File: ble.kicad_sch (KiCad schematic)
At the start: 0 parts

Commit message: schema functionally done
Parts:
- added C19, C21: 12pF, Capacitor_SMD:C_0805_2012Metric, symbol Device:C
- added C22: 100nF, Capacitor_SMD:C_0805_2012Metric, symbol Device:C
- added C23: 4.7uF, Capacitor_SMD:C_0805_2012Metric, symbol Device:C
- added MOD1: BT832A, footprints:BT832A, symbol user:BT832A
- added Y1: FC-135 32.7680KA-AC0, Crystal:Crystal_SMD_3215-2Pin_3.2x1.5mm, symbol Device:Crystal
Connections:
- new net: C21.2, MOD1.4 (P001/XL2), Y1.1
- new net: C19.2, MOD1.3 (P000/XL1), Y1.2
- new net +3V0: C22.1, C23.1, MOD1.9 (VDD)
- new net BLE_RESET: MOD1.14 (P021/RESET)
- new net BLE_SCL: MOD1.2 (P027/SCL)
- new net BLE_SDA: MOD1.1 (P026/SDA)
- new net GND: C19.1, C21.1, C22.2, C23.2, MOD1.10 (GND)
- new net SWCLK: MOD1.15 (SWCLK)
- new net SWD: MOD1.16 (SWDIO)
- no-connect marks 0 -> 7

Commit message: reannotation
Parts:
- renumbered C19 to C21, C21 to C22, C22 to C23, C23 to C24, Y1 to Y2

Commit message: schematic cleanup
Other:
- moved on the sheet: C21, C23, C24, Y2

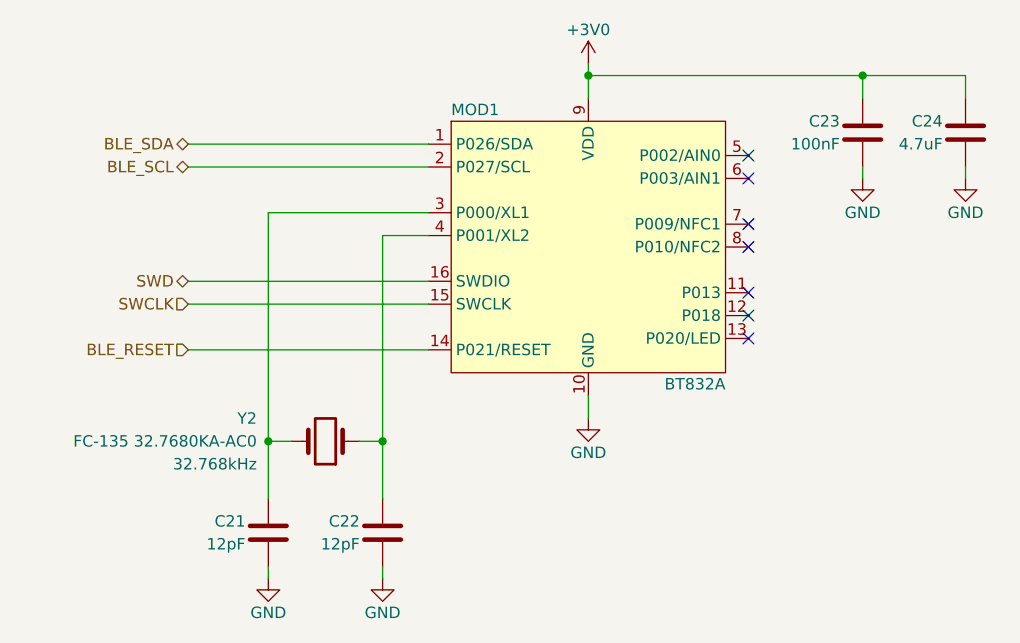
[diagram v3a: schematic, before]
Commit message: added testpoints
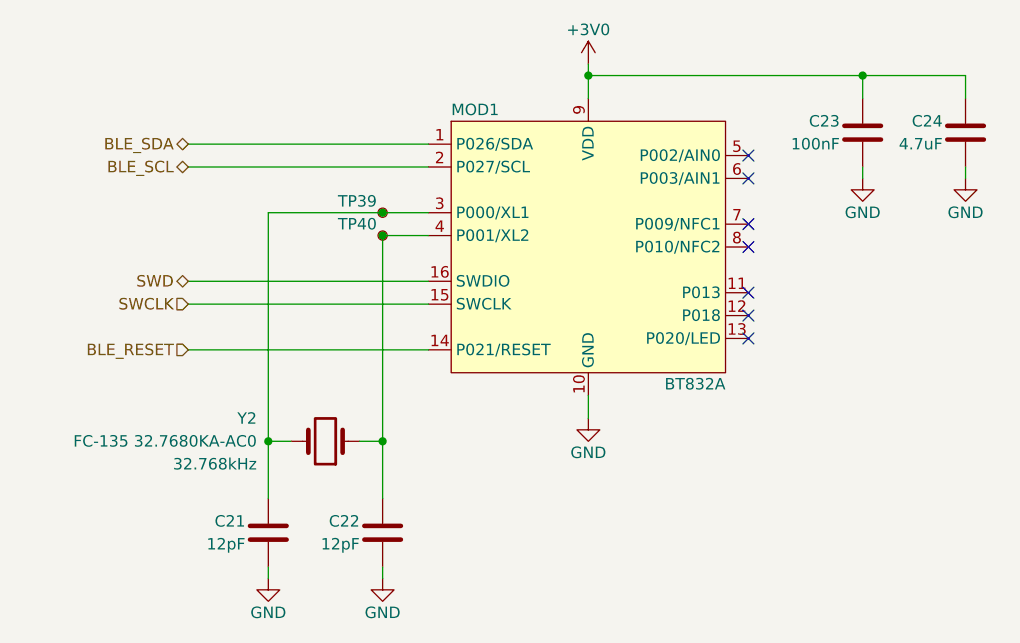
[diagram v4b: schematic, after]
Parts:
- added TP39, TP40: TestPoint_Small, TestPoint:TestPoint_Pad_D2.0mm, symbol Connector:TestPoint_Small
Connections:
- net at C22.2, MOD1.4 (P001/XL2), Y2.1: now also TP40.1
- net at C21.2, MOD1.3 (P000/XL1), Y2.2: now also TP39.1

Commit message: test points
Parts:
- removed TP39, TP40: TestPoint_Small, TestPoint:TestPoint_Pad_D2.0mm, symbol Connector:TestPoint_Small
- added TP48: BX1, TestPoint:TestPoint_Pad_D2.0mm, symbol Connector:TestPoint_Small
- added TP49: BX2, TestPoint:TestPoint_Pad_D2.0mm, symbol Connector:TestPoint_Small
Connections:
- net at C22.2, MOD1.4 (P001/XL2), Y2.1: now also TP49.1
- net at C21.2, MOD1.3 (P000/XL1), Y2.2: now also TP48.1

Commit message: GPIO shuffling + reannotate
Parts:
- renumbered TP48 to TP49, TP49 to TP50
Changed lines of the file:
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@@
   (symbol (lib_id "Connector:TestPoint_Small") (at 123.19 91.44 0) (mirror y) (unit 1)
     (in_bom yes) (on_board yes) (dnp no)
-    (property "Reference" "TP48" (at 122.555 90.17 0)
+    (property "Reference" "TP49" (at 122.555 90.17 0)
       (effects (font (size 1.27 1.27)) (justify left) hide)
     )
@@
       (project "gkos_pebble"
         (path "/ab6fff6e-44fa-4992-ab9d-8d9a7df4367d/f1e179d9-6d1d-4136-839e-ba1cd3485093"
-          (reference "TP48") (unit 1)
+          (reference "TP49") (unit 1)
         )
       )
@@
   (symbol (lib_id "Connector:TestPoint_Small") (at 123.19 93.98 0) (mirror y) (unit 1)
     (in_bom yes) (on_board yes) (dnp no)
-    (property "Reference" "TP49" (at 122.555 92.71 0)
+    (property "Reference" "TP50" (at 122.555 92.71 0)
       (effects (font (size 1.27 1.27)) (justify left) hide)
     )
@@
       (project "gkos_pebble"
         (path "/ab6fff6e-44fa-4992-ab9d-8d9a7df4367d/f1e179d9-6d1d-4136-839e-ba1cd3485093"
-          (reference "TP49") (unit 1)
-        )
-      )
+          (reference "TP50") (unit 1)
+        )
+      )

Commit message: in progress pcb
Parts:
- C21, C22, C23, C24: footprint Capacitor_SMD:C_0805_2012Metric -> Capacitor_SMD:C_0603_1608Metric
- TP49, TP50: footprint TestPoint:TestPoint_Pad_D2.0mm -> TestPoint:TestPoint_Pad_D1.0mm
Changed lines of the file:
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@@
       (effects (font (size 1.27 1.27)) (justify left))
     )
-    (property "Footprint" "TestPoint:TestPoint_Pad_D2.0mm" (at 118.11 91.44 0)
+    (property "Footprint" "TestPoint:TestPoint_Pad_D1.0mm" (at 118.11 91.44 0)
       (effects (font (size 1.27 1.27)) hide)
     )
@@
       (effects (font (size 1.27 1.27)) (justify right))
     )
-    (property "Footprint" "Capacitor_SMD:C_0805_2012Metric" (at 111.4552 123.19 0)
+    (property "Footprint" "Capacitor_SMD:C_0603_1608Metric" (at 111.4552 123.19 0)
       (effects (font (size 1.27 1.27)) hide)
     )
@@
       (effects (font (size 1.27 1.27)) (justify right))
     )
-    (property "Footprint" "Capacitor_SMD:C_0805_2012Metric" (at 188.9252 86.36 0)
+    (property "Footprint" "Capacitor_SMD:C_0603_1608Metric" (at 188.9252 86.36 0)
       (effects (font (size 1.27 1.27)) hide)
     )
@@
       (effects (font (size 1.27 1.27)) (justify right))
     )
-    (property "Footprint" "Capacitor_SMD:C_0805_2012Metric" (at 124.1552 123.19 0)
+    (property "Footprint" "Capacitor_SMD:C_0603_1608Metric" (at 124.1552 123.19 0)
       (effects (font (size 1.27 1.27)) hide)
     )
@@
       (effects (font (size 1.27 1.27)) (justify right))
     )
-    (property "Footprint" "Capacitor_SMD:C_0805_2012Metric" (at 177.4952 86.36 0)
+    (property "Footprint" "Capacitor_SMD:C_0603_1608Metric" (at 177.4952 86.36 0)
       (effects (font (size 1.27 1.27)) hide)
     )
@@
       (effects (font (size 1.27 1.27)) (justify left))
     )
-    (property "Footprint" "TestPoint:TestPoint_Pad_D2.0mm" (at 118.11 93.98 0)
-      (effects (font (size 1.27 1.27)) hide)
-    )
+    (property "Footprint" "TestPoint:TestPoint_Pad_D1.0mm" (at 118.11 93.98 0)
+      (effects (font (size 1.27 1.27)) hide)
+    )

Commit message: add the dang eeprom
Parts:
- renumbered TP49 to TP48, TP50 to TP49
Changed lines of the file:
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@@
   (symbol (lib_id "power:+3V0") (at 146.05 74.93 0) (unit 1)
     (in_bom yes) (on_board yes) (dnp no)
-    (property "Reference" "#PWR034" (at 146.05 78.74 0)
+    (property "Reference" "#PWR036" (at 146.05 78.74 0)
       (effects (font (size 1.27 1.27)) hide)
     )
@@
       (project "gkos_pebble"
         (path "/ab6fff6e-44fa-4992-ab9d-8d9a7df4367d/f1e179d9-6d1d-4136-839e-ba1cd3485093"
-          (reference "#PWR034") (unit 1)
+          (reference "#PWR036") (unit 1)
         )
       )
@@
   (symbol (lib_id "Connector:TestPoint_Small") (at 123.19 91.44 0) (mirror y) (unit 1)
     (in_bom yes) (on_board yes) (dnp no)
-    (property "Reference" "TP49" (at 122.555 90.17 0)
+    (property "Reference" "TP48" (at 122.555 90.17 0)
       (effects (font (size 1.27 1.27)) (justify left) hide)
     )
@@
       (project "gkos_pebble"
         (path "/ab6fff6e-44fa-4992-ab9d-8d9a7df4367d/f1e179d9-6d1d-4136-839e-ba1cd3485093"
-          (reference "TP49") (unit 1)
+          (reference "TP48") (unit 1)
         )
       )
@@
   (symbol (lib_id "power:GND") (at 187.96 87.63 0) (unit 1)
     (in_bom yes) (on_board yes) (dnp no)
-    (property "Reference" "#PWR037" (at 187.96 93.98 0)
+    (property "Reference" "#PWR039" (at 187.96 93.98 0)
       (effects (font (size 1.27 1.27)) hide)
     )
@@
       (project "gkos_pebble"
         (path "/ab6fff6e-44fa-4992-ab9d-8d9a7df4367d/f1e179d9-6d1d-4136-839e-ba1cd3485093"
+          (reference "#PWR039") (unit 1)
+        )
+      )
+    )
+  )
+  (symbol (lib_id "power:GND") (at 146.05 114.3 0) (unit 1)
+    (in_bom yes) (on_board yes) (dnp no)
+    (property "Reference" "#PWR037" (at 146.05 120.65 0)
+      (effects (font (size 1.27 1.27)) hide)
+    )
+    (property "Value" "GND" (at 146.05 118.11 0)
+      (effects (font (size 1.27 1.27)))
+    )
+    (property "Footprint" "" (at 146.05 114.3 0)
+      (effects (font (size 1.27 1.27)) hide)
+    )
+    (property "Datasheet" "" (at 146.05 114.3 0)
+      (effects (font (size 1.27 1.27)) hide)
+    )
+    (pin "1")
+    (instances
+      (project "gkos_pebble"
+        (path "/ab6fff6e-44fa-4992-ab9d-8d9a7df4367d/f1e179d9-6d1d-4136-839e-ba1cd3485093"
           (reference "#PWR037") (unit 1)
         )
@@
     )
   )
-  (symbol (lib_id "power:GND") (at 146.05 114.3 0) (unit 1)
-    (in_bom yes) (on_board yes) (dnp no)
-    (property "Reference" "#PWR035" (at 146.05 120.65 0)
-      (effects (font (size 1.27 1.27)) hide)
-    )
-    (property "Value" "GND" (at 146.05 118.11 0)
-      (effects (font (size 1.27 1.27)))
-    )
-    (property "Footprint" "" (at 146.05 114.3 0)
-      (effects (font (size 1.27 1.27)) hide)
-    )
-    (property "Datasheet" "" (at 146.05 114.3 0)
+  (symbol (lib_id "power:GND") (at 176.53 87.63 0) (mirror y) (unit 1)
+    (in_bom yes) (on_board yes) (dnp no)
+    (property "Reference" "#PWR038" (at 176.53 93.98 0)
+      (effects (font (size 1.27 1.27)) hide)
+    )
+    (property "Value" "GND" (at 176.53 91.44 0)
+      (effects (font (size 1.27 1.27)))
+    )
+    (property "Footprint" "" (at 176.53 87.63 0)
+      (effects (font (size 1.27 1.27)) hide)
+    )
+    (property "Datasheet" "" (at 176.53 87.63 0)
+      (effects (font (size 1.27 1.27)) hide)
+    )
+    (pin "1")
+    (instances
+      (project "gkos_pebble"
+        (path "/ab6fff6e-44fa-4992-ab9d-8d9a7df4367d/f1e179d9-6d1d-4136-839e-ba1cd3485093"
+          (reference "#PWR038") (unit 1)
+        )
+      )
+    )
+  )
+  (symbol (lib_id "power:GND") (at 123.19 132.08 0) (unit 1)
+    (in_bom yes) (on_board yes) (dnp no)
+    (property "Reference" "#PWR035" (at 123.19 138.43 0)
+      (effects (font (size 1.27 1.27)) hide)
+    )
+    (property "Value" "GND" (at 123.19 135.89 0)
+      (effects (font (size 1.27 1.27)))
+    )
+    (property "Footprint" "" (at 123.19 132.08 0)
+      (effects (font (size 1.27 1.27)) hide)
+    )
+    (property "Datasheet" "" (at 123.19 132.08 0)
       (effects (font (size 1.27 1.27)) hide)
     )
@@
     )
   )
-  (symbol (lib_id "power:GND") (at 176.53 87.63 0) (mirror y) (unit 1)
-    (in_bom yes) (on_board yes) (dnp no)
-    (property "Reference" "#PWR036" (at 176.53 93.98 0)
-      (effects (font (size 1.27 1.27)) hide)
-    )
-    (property "Value" "GND" (at 176.53 91.44 0)
-      (effects (font (size 1.27 1.27)))
-    )
-    (property "Footprint" "" (at 176.53 87.63 0)
-      (effects (font (size 1.27 1.27)) hide)
-    )
-    (property "Datasheet" "" (at 176.53 87.63 0)
-      (effects (font (size 1.27 1.27)) hide)
-    )
-    (pin "1")
-    (instances
-      (project "gkos_pebble"
-        (path "/ab6fff6e-44fa-4992-ab9d-8d9a7df4367d/f1e179d9-6d1d-4136-839e-ba1cd3485093"
-          (reference "#PWR036") (unit 1)
-        )
-      )
-    )
-  )
-  (symbol (lib_id "power:GND") (at 123.19 132.08 0) (unit 1)
-    (in_bom yes) (on_board yes) (dnp no)
-    (property "Reference" "#PWR033" (at 123.19 138.43 0)
-      (effects (font (size 1.27 1.27)) hide)
-    )
-    (property "Value" "GND" (at 123.19 135.89 0)
-      (effects (font (size 1.27 1.27)))
-    )
-    (property "Footprint" "" (at 123.19 132.08 0)
-      (effects (font (size 1.27 1.27)) hide)
-    )
-    (property "Datasheet" "" (at 123.19 132.08 0)
-      (effects (font (size 1.27 1.27)) hide)
-    )
-    (pin "1")
-    (instances
-      (project "gkos_pebble"
-        (path "/ab6fff6e-44fa-4992-ab9d-8d9a7df4367d/f1e179d9-6d1d-4136-839e-ba1cd3485093"
-          (reference "#PWR033") (unit 1)
-        )
-      )
-    )
-  )
   (symbol (lib_id "Device:C") (at 176.53 82.55 0) (unit 1)
     (in_bom yes) (on_board yes) (dnp no)
@@
   (symbol (lib_id "Connector:TestPoint_Small") (at 123.19 93.98 0) (mirror y) (unit 1)
     (in_bom yes) (on_board yes) (dnp no)
-    (property "Reference" "TP50" (at 122.555 92.71 0)
+    (property "Reference" "TP49" (at 122.555 92.71 0)
       (effects (font (size 1.27 1.27)) (justify left) hide)
     )
@@
       (project "gkos_pebble"
         (path "/ab6fff6e-44fa-4992-ab9d-8d9a7df4367d/f1e179d9-6d1d-4136-839e-ba1cd3485093"
-          (reference "TP50") (unit 1)
+          (reference "TP49") (unit 1)
         )
       )
@@
   (symbol (lib_id "power:GND") (at 110.49 132.08 0) (unit 1)
     (in_bom yes) (on_board yes) (dnp no)
-    (property "Reference" "#PWR032" (at 110.49 138.43 0)
+    (property "Reference" "#PWR034" (at 110.49 138.43 0)
       (effects (font (size 1.27 1.27)) hide)
     )
@@
       (project "gkos_pebble"
         (path "/ab6fff6e-44fa-4992-ab9d-8d9a7df4367d/f1e179d9-6d1d-4136-839e-ba1cd3485093"
-          (reference "#PWR032") (unit 1)
-        )
-      )
+          (reference "#PWR034") (unit 1)
+        )
+      )
